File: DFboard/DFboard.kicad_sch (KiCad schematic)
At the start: 16 parts, among them J1 DB25_Plug_MountingHoles_Male, J13 110-43-648-41-001000, J2 DB25_Receptacle_MountingHoles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, U1 Power, U6 Power

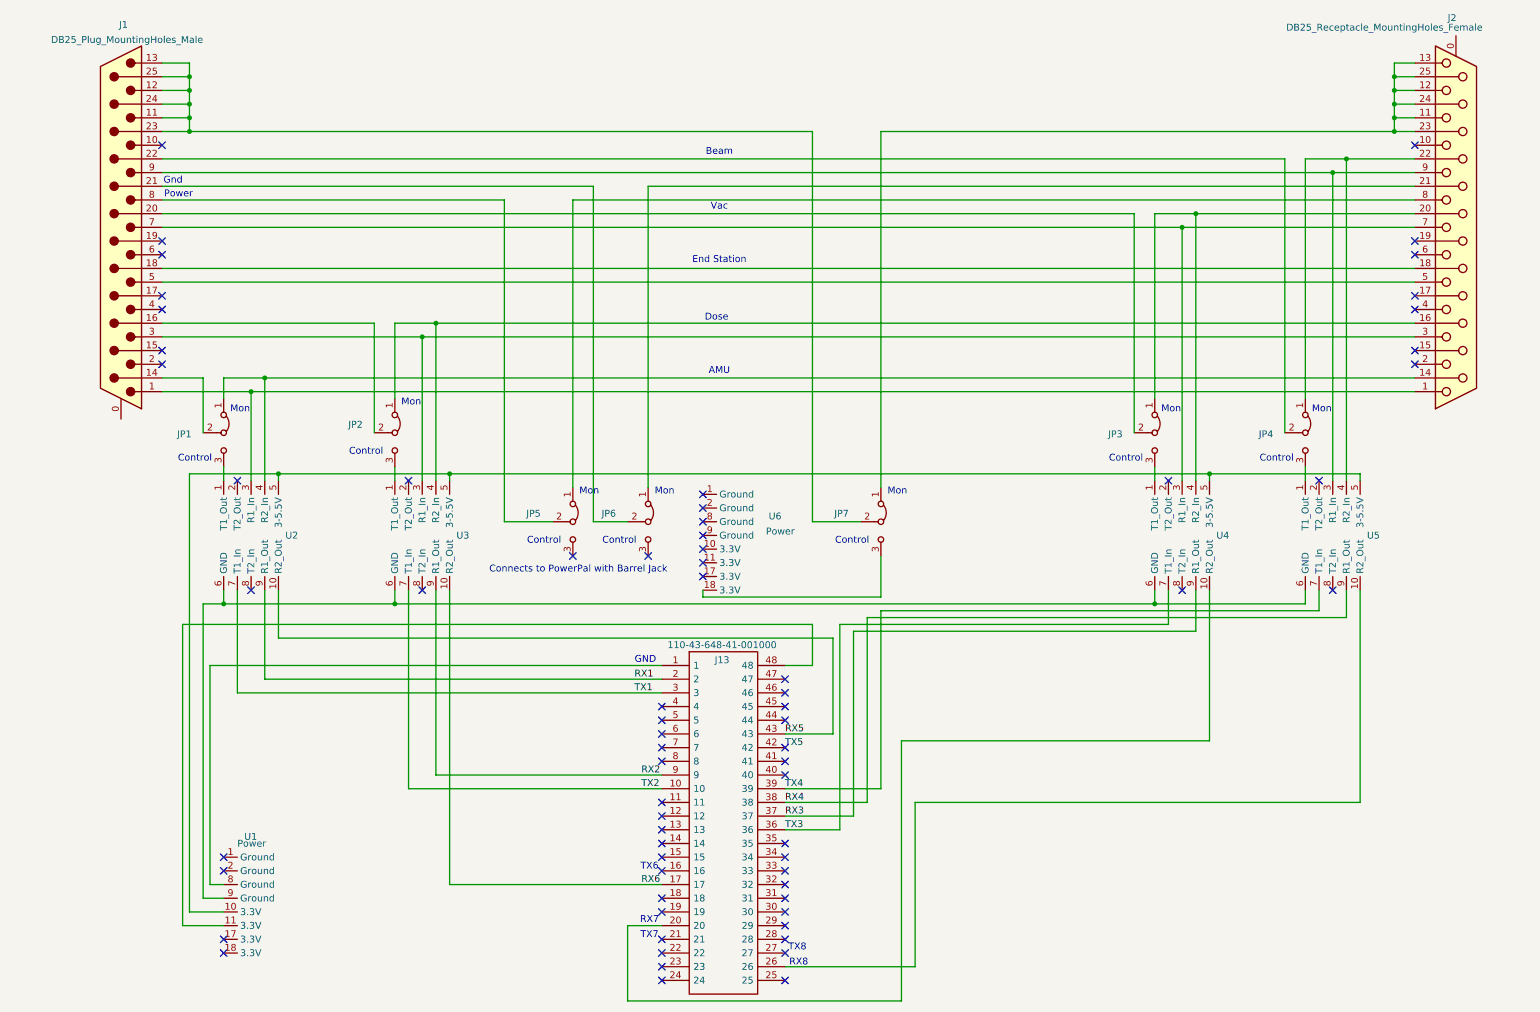
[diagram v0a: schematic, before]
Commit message: Added test points to schematic.  Started pcb layout.
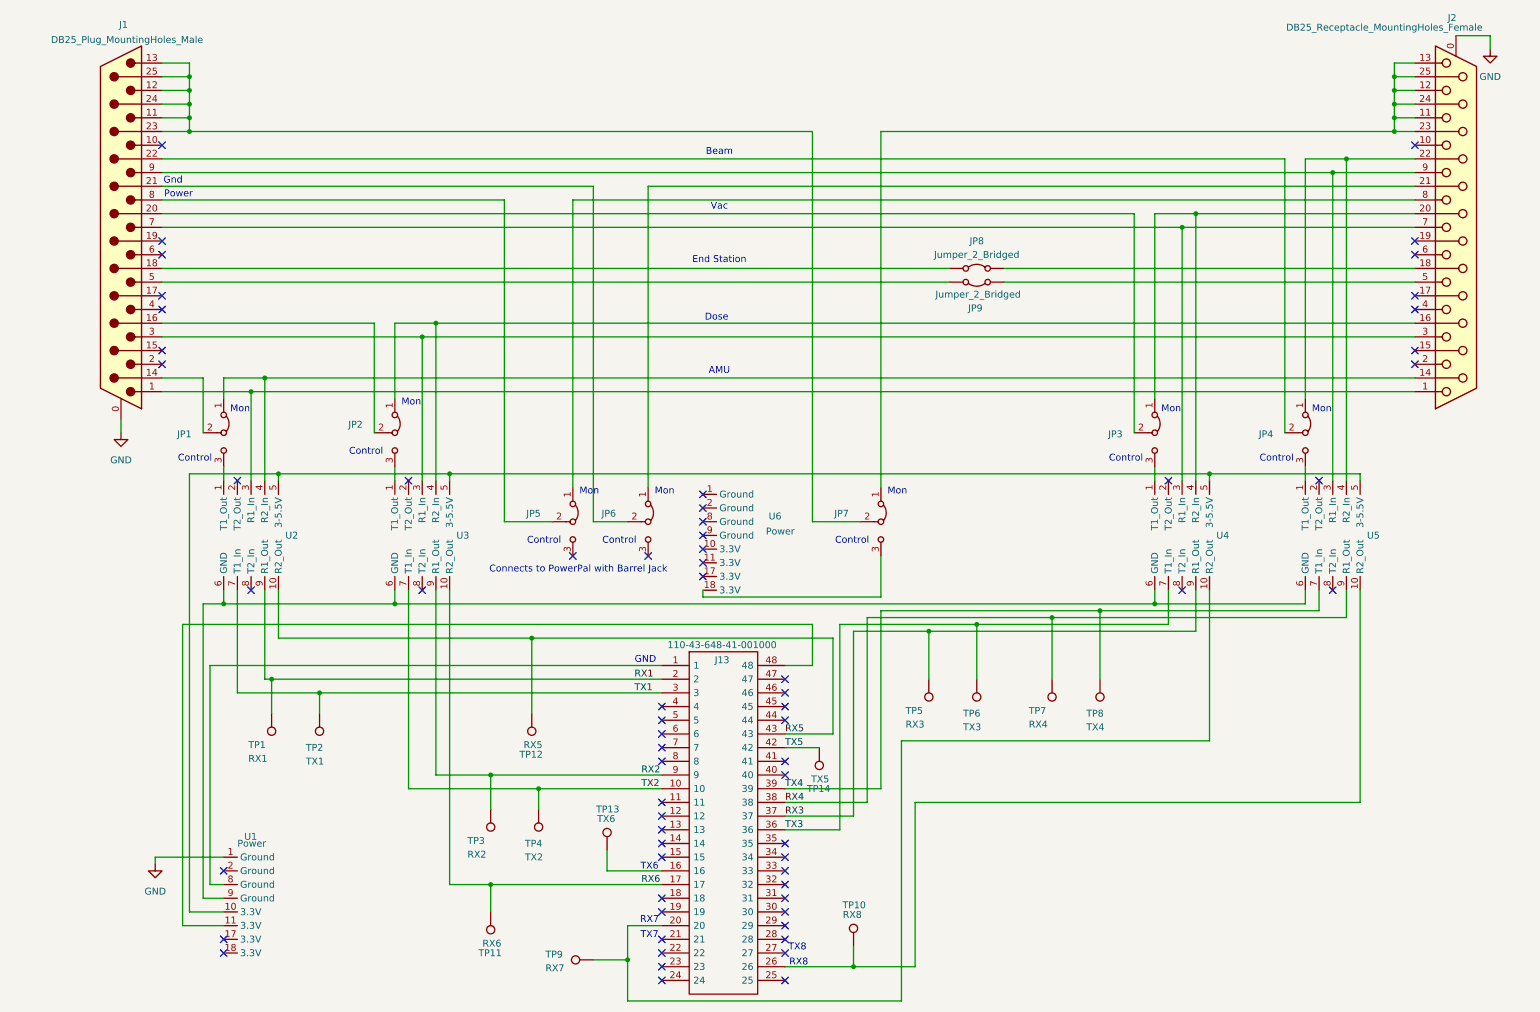
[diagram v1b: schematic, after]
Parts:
- added JP8, JP9: Jumper_2_Bridged, Connector_PinHeader_2.54mm:PinHeader_1x02_P2.54mm_Vertical, symbol Jumper:Jumper_2_Bridged
- added TP1: RX1, Connector_PinHeader_2.54mm:PinHeader_1x01_P2.54mm_Vertical, symbol Connector:TestPoint
- added TP10: RX8, Connector_PinHeader_2.54mm:PinHeader_1x01_P2.54mm_Vertical, symbol Connector:TestPoint
- added TP11: RX6, Connector_PinHeader_2.54mm:PinHeader_1x01_P2.54mm_Vertical, symbol Connector:TestPoint
- added TP12: RX5, Connector_PinHeader_2.54mm:PinHeader_1x01_P2.54mm_Vertical, symbol Connector:TestPoint
- added TP13: TX6, Connector_PinHeader_2.54mm:PinHeader_1x01_P2.54mm_Vertical, symbol Connector:TestPoint
- added TP14: TX5, Connector_PinHeader_2.54mm:PinHeader_1x01_P2.54mm_Vertical, symbol Connector:TestPoint
- added TP2: TX1, Connector_PinHeader_2.54mm:PinHeader_1x01_P2.54mm_Vertical, symbol Connector:TestPoint
- added TP3: RX2, Connector_PinHeader_2.54mm:PinHeader_1x01_P2.54mm_Vertical, symbol Connector:TestPoint
- added TP4: TX2, Connector_PinHeader_2.54mm:PinHeader_1x01_P2.54mm_Vertical, symbol Connector:TestPoint
- added TP5: RX3, Connector_PinHeader_2.54mm:PinHeader_1x01_P2.54mm_Vertical, symbol Connector:TestPoint
- added TP6: TX3, Connector_PinHeader_2.54mm:PinHeader_1x01_P2.54mm_Vertical, symbol Connector:TestPoint
- added TP7: RX4, Connector_PinHeader_2.54mm:PinHeader_1x01_P2.54mm_Vertical, symbol Connector:TestPoint
- added TP8: TX4, Connector_PinHeader_2.54mm:PinHeader_1x01_P2.54mm_Vertical, symbol Connector:TestPoint
- added TP9: RX7, Connector_PinHeader_2.54mm:PinHeader_1x01_P2.54mm_Vertical, symbol Connector:TestPoint
- J1: footprint (none) -> Connector_Dsub:DSUB-25_Male_Horizontal_P2.77x2.84mm_EdgePinOffset4.94mm_Housed_MountingHolesOffset7.48mm
- J2: footprint (none) -> Connector_Dsub:DSUB-25_Female_Horizontal_P2.77x2.84mm_EdgePinOffset4.94mm_Housed_MountingHolesOffset7.48mm
- JP1, JP2, JP3, JP4, JP5, JP6, JP7: footprint (none) -> Connector_PinHeader_2.54mm:PinHeader_1x03_P2.54mm_Vertical
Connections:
- net RX1: now also TP1.1
- net RX2: now also TP3.1
- net RX3: now also TP5.1
- net RX4: now also TP7.1
- net RX5: now also TP12.1
- net RX6: now also TP11.1
- net TX1: now also TP2.1
- net TX2: now also TP4.1
- net TX3: now also TP6.1
- net TX4: now also TP8.1
- net TX5: now also TP14.1
- net GND: now reaches J1.0 (PAD)
- net GND: now also J2.0 (PAD), U1.1 (Ground)
- net at J1.18 (P18): now also JP8.1 (A); no longer J2.18 (P18)
- net at J1.5: now also JP9.2 (B); no longer J2.5
- net at J13.26, U5.10 (R2_Out): now also TP10.1
- net at J13.20, U4.10 (R2_Out): now also TP9.1
- net at J13.16: now also TP13.1
- new net: J2.5, JP9.1 (A)
- new net: J2.18 (P18), JP8.2 (B)
- no-connect marks 69 -> 66

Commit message: Board version 0.2 - fixed missing ground
The ground for the PowerPal was not connected to the ground coming from the implanter and the signals were all over the place.
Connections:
- net at J1.21 (P21), JP6.2 (C): now also U1.9 (Ground), U2.6 (GND), U3.6 (GND), U4.6 (GND), U5.6 (GND), U6.2 (Ground)
- no-connect marks 66 -> 65
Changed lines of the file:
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@@
+	)
+	(junction
+		(at 115.57 121.92)
+		(diameter 0)
+		(color 0 0 0 0)
 	)
 	(junction
@@
 	)
 	(junction
+		(at 115.57 106.68)
+		(diameter 0)
+		(color 0 0 0 0)
+	)
+	(junction
 		(at 264.16 29.21)
 		(diameter 0)
@@
 	)
 	(junction
+		(at 115.57 118.11)
+		(diameter 0)
+		(color 0 0 0 0)
+	)
+	(junction
 		(at 264.16 31.75)
 		(diameter 0)
@@
 	)
 	(no_connect
+		(at 128.27 184.15)
+	)
+	(no_connect
+		(at 222.25 99.06)
+	)
+	(no_connect
+		(at 267.97 54.61)
+	)
+	(no_connect
+		(at 46.99 186.69)
+	)
+	(no_connect
+		(at 252.73 119.38)
+	)
+	(no_connect
+		(at 224.79 119.38)
+	)
+	(no_connect
+		(at 128.27 140.97)
+	)
+	(no_connect
+		(at 135.89 109.22)
+	)
+	(no_connect
+		(at 267.97 74.93)
+	)
+	(no_connect
+		(at 125.73 113.03)
+	)
+	(no_connect
+		(at 267.97 67.31)
+	)
+	(no_connect
+		(at 81.28 99.06)
+	)
+	(no_connect
+		(at 35.56 54.61)
+	)
+	(no_connect
 		(at 135.89 101.6)
 	)
-	(no_connect
-		(at 128.27 184.15)
-	)
-	(no_connect
-		(at 222.25 99.06)
-	)
-	(no_connect
-		(at 267.97 54.61)
-	)
-	(no_connect
-		(at 46.99 186.69)
-	)
-	(no_connect
-		(at 252.73 119.38)
-	)
-	(no_connect
-		(at 135.89 104.14)
-	)
-	(no_connect
-		(at 224.79 119.38)
-	)
-	(no_connect
-		(at 128.27 140.97)
-	)
-	(no_connect
-		(at 135.89 109.22)
-	)
-	(no_connect
-		(at 267.97 74.93)
-	)
-	(no_connect
-		(at 125.73 113.03)
-	)
-	(no_connect
-		(at 267.97 67.31)
-	)
-	(no_connect
-		(at 81.28 99.06)
-	)
-	(no_connect
-		(at 35.56 54.61)
-	)
 	(wire
 		(pts
@@
 	(wire
 		(pts
+			(xy 133.35 118.11) (xy 133.35 104.14)
+		)
+		(stroke
+			(width 0)
+			(type default)
+		)
+	)
+	(wire
+		(pts
 			(xy 78.74 69.85) (xy 86.36 69.85)
 		)
@@
 	(wire
 		(pts
+			(xy 115.57 118.11) (xy 115.57 121.92)
+		)
+		(stroke
+			(width 0)
+			(type default)
+		)
+	)
+	(wire
+		(pts
 			(xy 267.97 21.59) (xy 264.16 21.59)
 		)
@@
 	(wire
 		(pts
+			(xy 115.57 106.68) (xy 115.57 118.11)
+		)
+		(stroke
+			(width 0)
+			(type default)
+		)
+	)
+	(wire
+		(pts
 			(xy 151.13 161.29) (xy 163.83 161.29)
 		)
@@
 	(wire
 		(pts
+			(xy 115.57 121.92) (xy 219.71 121.92)
+		)
+		(stroke
+			(width 0)
+			(type default)
+		)
+	)
+	(wire
+		(pts
 			(xy 161.29 163.83) (xy 161.29 125.73)
 		)
@@
 	(wire
 		(pts
-			(xy 78.74 121.92) (xy 219.71 121.92)
+			(xy 78.74 121.92) (xy 115.57 121.92)
 		)
 		(stroke
@@
 	(wire
 		(pts
+			(xy 133.35 118.11) (xy 115.57 118.11)
+		)
+		(stroke
+			(width 0)
+			(type default)
+		)
+	)
+	(wire
+		(pts
 			(xy 35.56 46.99) (xy 99.06 46.99)
 		)
@@
 		)
 		(stroke
+			(width 0)
+			(type default)
+		)
+	)
+	(wire
+		(pts
+			(xy 133.35 104.14) (xy 135.89 104.14)
+		)
+		(stroke
